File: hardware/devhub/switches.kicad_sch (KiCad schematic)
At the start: 18 parts, among them U4 TPS2561ADRC, U5 TPS2561ADRC, U6 TPS2561ADRC, U7 INA3221, U8 INA3221

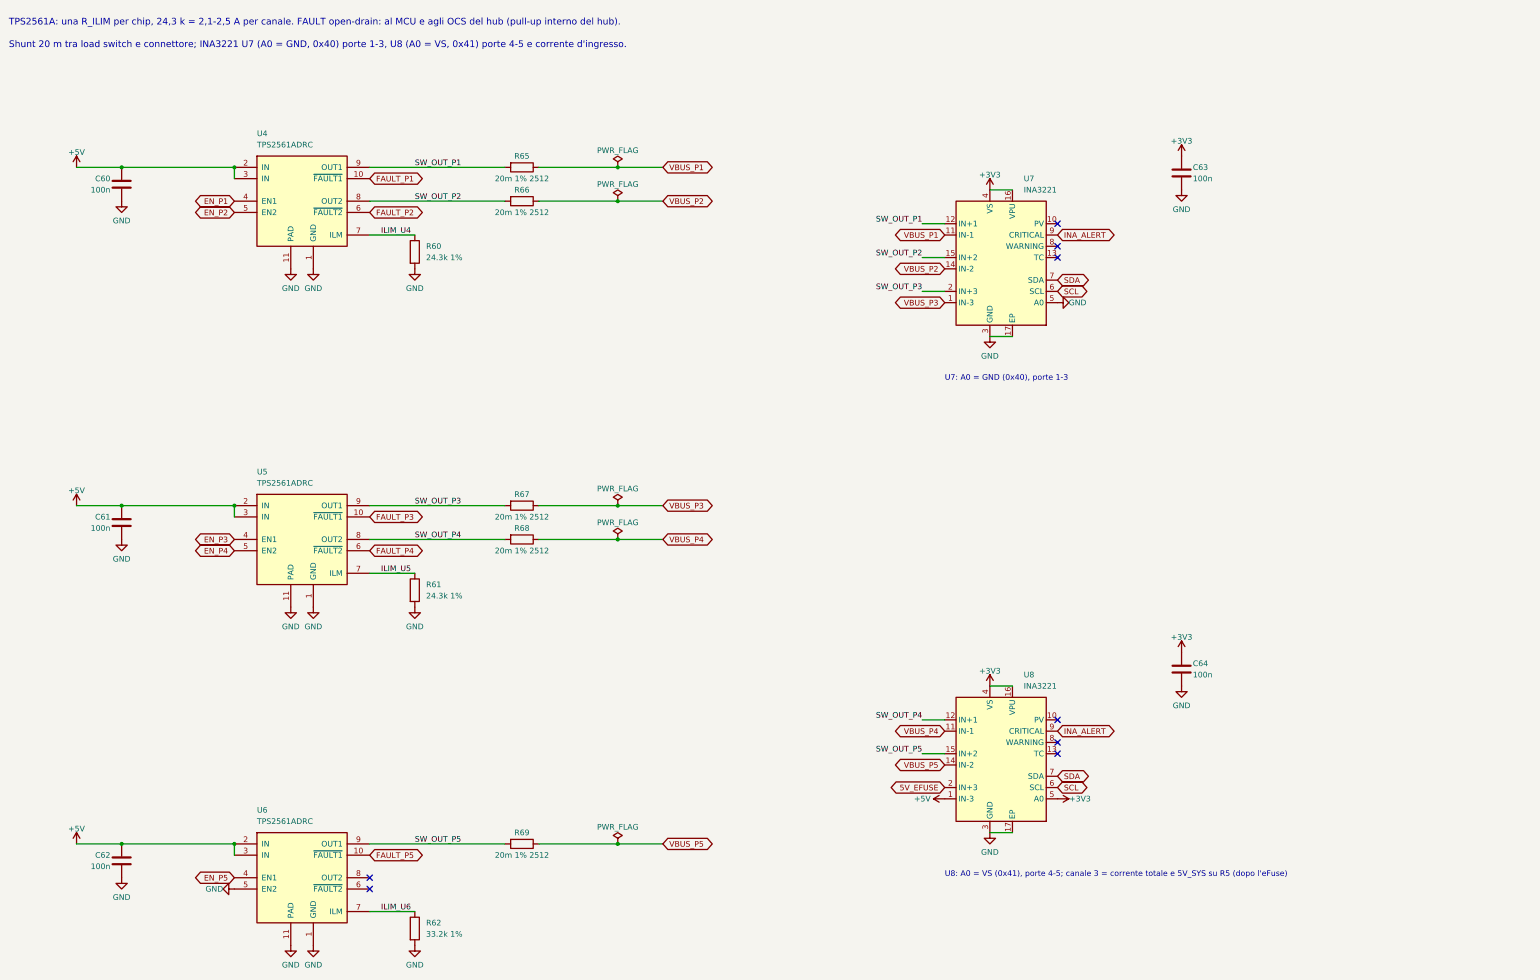
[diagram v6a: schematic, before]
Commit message: Schematic v0.3: apply simplified requirements (D79-D81)
Update the existing KiCad project instead of starting over:
- MCU U3 replaced with STM32G0B1CEU6 (UFQFPN48) on the 48-pin pinout
- switches sheet: two UCS2114-1-V/LX on separate I2C buses replace
  TPS2561A, INA3221 and current shunts
- ports: single MCU-driven LED, discrete VBUS discharge removed
- remove USB-A port, spare hub header, second relay channel,
  input CC ADC filters and input shunt
- add UCS2114 symbol and footprint (Microchip land pattern C04-2421)
- align pinout, decisions, architecture and component docs
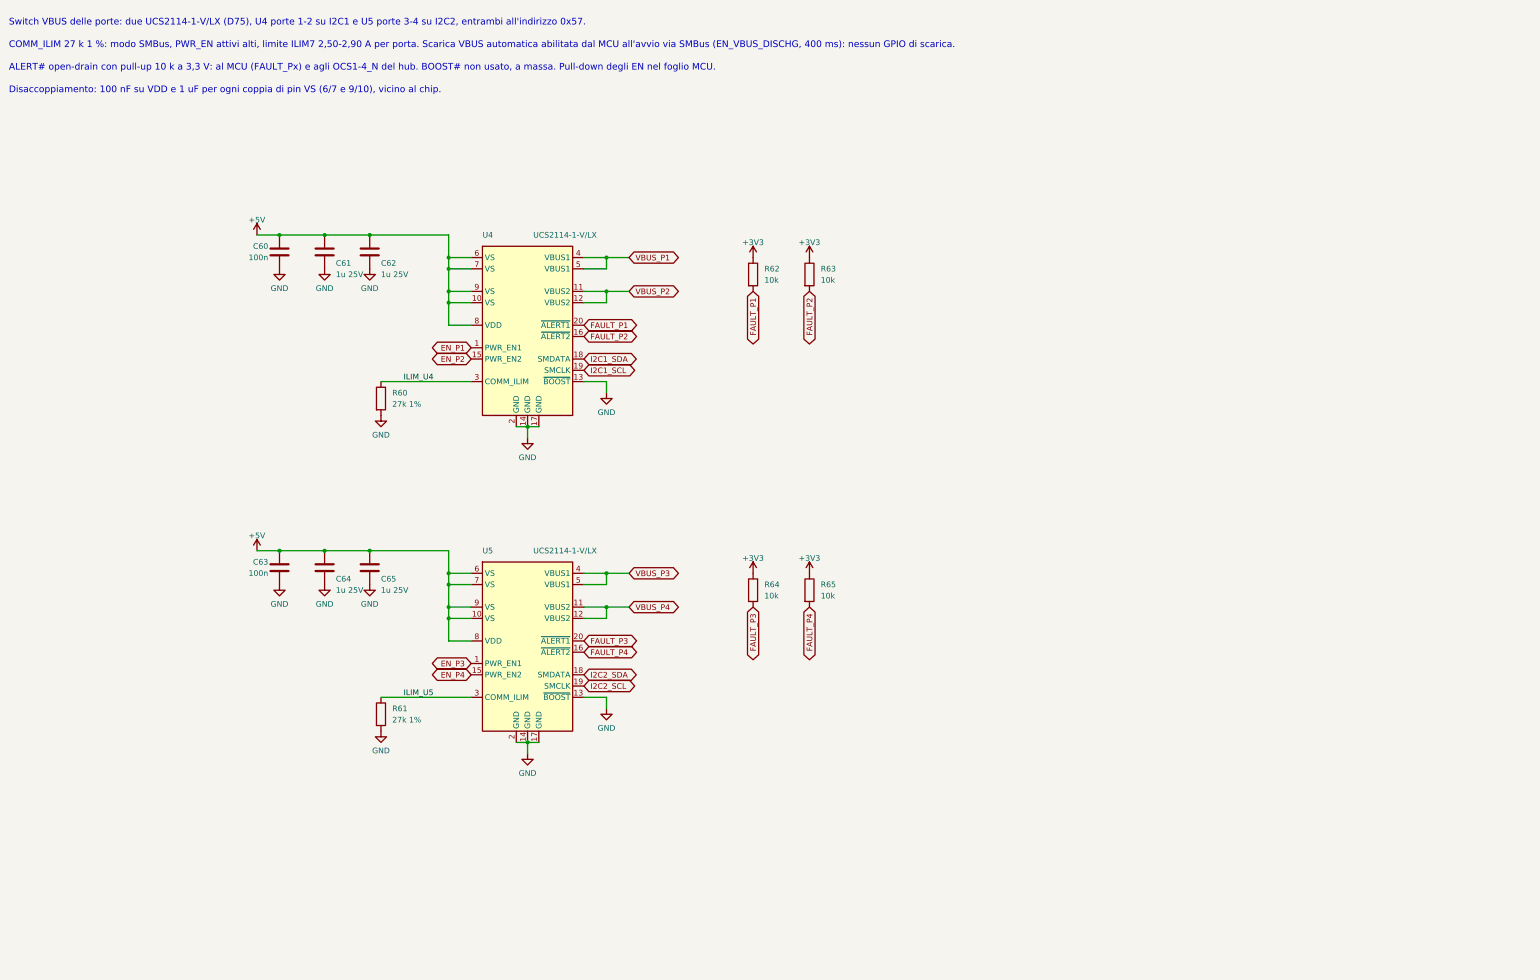
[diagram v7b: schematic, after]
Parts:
- removed R66, R67, R68, R69: 20m 1% 2512, Resistor_SMD:R_2512_6332Metric, symbol Device:R
- removed U4, U5, U6: TPS2561ADRC, Package_SON:VSON-10-1EP_3x3mm_P0.5mm_EP1.65x2.4mm_ThermalVias, symbol Interface_USB:TPS2561
- removed U7, U8: INA3221, Package_DFN_QFN:Texas_RGV0016A_VQFN-16-1EP_4x4mm_P0.65mm_EP2.1x2.1mm, symbol Power_Management:INA3221
- added C65: 1u 25V, Capacitor_SMD:C_0603_1608Metric, symbol Device:C
- added R63, R64: 10k, Resistor_SMD:R_0603_1608Metric, symbol Device:R
- added U4, U5: UCS2114-1-V/LX, lcsc_footprints:UCS2114_VQFN-20_3x3mm_P0.5mm, symbol devhub:UCS2114
- C61, C62, C64: value 100n -> 1u 25V; digikey 1276-1000-1-ND -> 1276-1184-1-ND; lcsc C1591 -> C29936; mouser 187-CL10B104KB8NNNC -> 187-CL10B105KA8NNNC; warehouse 235 -> 240
- R60, R61: value 24.3k 1% -> 27k 1%; digikey 311-24.3KHRCT-ND -> 311-27.0KHRCT-ND; lcsc C276290 -> (none); mouser 603-RC0603FR-0724K3L -> 603-RC0603FR-0727KL
- R62: value 33.2k 1% -> 10k; digikey 311-33.2KHRCT-ND -> 311-10.0KHRCT-ND; lcsc C185338 -> C2906982; mouser 603-RC0603FR-0733K2L -> 603-RC0603FR-0710KL; warehouse (none) -> 248
- R65: value 20m 1% 2512 -> 10k; footprint Resistor_SMD:R_2512_6332Metric -> Resistor_SMD:R_0603_1608Metric; digikey 311-0.02TCT-ND -> 311-10.0KHRCT-ND; lcsc C326611 -> C2906982; mouser 603-RL2512FK-070R02L -> 603-RC0603FR-0710KL; warehouse (none) -> 248
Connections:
- net ILIM_U6 is gone; now on net +3V3: R62.1
- net SW_OUT_P1 is gone; now on net FAULT_P4: R65.2
- net +3V3: now also R65.1, R63.1, R64.1; no longer C63.1, C64.1
- net +5V: now also C63.1, C64.1, C65.1, U4.10 (VS), U4.6 (VS), U4.7 (VS), U4.8 (VDD), U4.9 (VS), U5.10 (VS), U5.6 (VS), U5.7 (VS), U5.8 (VDD), U5.9 (VS)
- net EN_P1: now also U4.1 (PWR_EN1)
- net EN_P2: now also U4.15 (PWR_EN2)
- net EN_P3: now also U5.1 (PWR_EN1)
- net EN_P4: now also U5.15 (PWR_EN2)
- net FAULT_P1: now also R62.2, U4.20 (~{ALERT1})
- net FAULT_P2: now also R63.2, U4.16 (~{ALERT2})
- net FAULT_P3: now also R64.2, U5.20 (~{ALERT1})
- net FAULT_P4: now also U5.16 (~{ALERT2})
- net GND: now also C65.2, U4.13 (~{BOOST}), U4.14 (GND), U4.17 (GND), U4.2 (GND), U5.13 (~{BOOST}), U5.14 (GND), U5.17 (GND), U5.2 (GND); no longer R62.2
- net ILIM_U4: now also U4.3 (COMM_ILIM)
- net ILIM_U5: now also U5.3 (COMM_ILIM)
- net VBUS_P1: now also U4.4 (VBUS1), U4.5 (VBUS1); no longer R65.1
- net VBUS_P2: now also U4.11 (VBUS2), U4.12 (VBUS2)
- net VBUS_P3: now also U5.4 (VBUS1), U5.5 (VBUS1)
- net VBUS_P4: now also U5.11 (VBUS2), U5.12 (VBUS2)
- new net I2C1_SCL: U4.19 (SMCLK)
- new net I2C1_SDA: U4.18 (SMDATA)
- new net I2C2_SCL: U5.19 (SMCLK)
- new net I2C2_SDA: U5.18 (SMDATA)
- no-connect marks 8 -> 0
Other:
- note added: "ALERT# open-drain con pull-up 10 k a 3,3 V: al MCU (FAULT_Px) e agli OCS1-4_N del hub. BOOST# non usato, a massa. Pull-down degli EN nel foglio MCU."
- note added: "COMM_ILIM 27 k 1 %: modo SMBus, PWR_EN attivi alti, limite ILIM7 2,50-2,90 A per porta. Scarica VBUS automatica abilitata dal MCU all'avvio via SMBus (EN_VBUS_DISCHG, 400 ms): nessun GPIO di scarica."
- note added: "Disaccoppiamento: 100 nF su VDD e 1 uF per ogni coppia di pin VS (6/7 e 9/10), vicino al chip."
- note added: "Switch VBUS delle porte: due UCS2114-1-V/LX (D75), U4 porte 1-2 su I2C1 e U5 porte 3-4 su I2C2, entrambi all'indirizzo 0x57."
- note removed: "Shunt 20 m tra load switch e connettore; INA3221 U7 (A0 = GND, 0x40) porte 1-3, U8 (A0 = VS, 0x41) porte 4-5 e corrente d'ingresso."
- note removed: "TPS2561A: una R_ILIM per chip, 24,3 k = 2,1-2,5 A per canale. FAULT open-drain: al MCU e agli OCS del hub (pull-up interno del hub)."
- note removed: "U7: A0 = GND (0x40), porte 1-3"
- note removed: "U8: A0 = VS (0x41), porte 4-5; canale 3 = corrente totale e 5V_SYS su R5 (dopo l'eFuse)"
- title: Load switch VBUS (TPS2561A) e misura di corrente (INA3221) -> Switch VBUS delle porte (UCS2114)
